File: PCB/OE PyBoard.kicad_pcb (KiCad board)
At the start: 4 copper layers, 33 x 41.9 mm, 57 parts, among them J3 USB4105-GF-A, J4 Conn_02x03_Odd_Even, J6 Conn_01x08, J7 Conn_01x08, U2 STM32F405RGT6, U3 MCP1700T, X2 12 MHz, X3 32.768 kHz

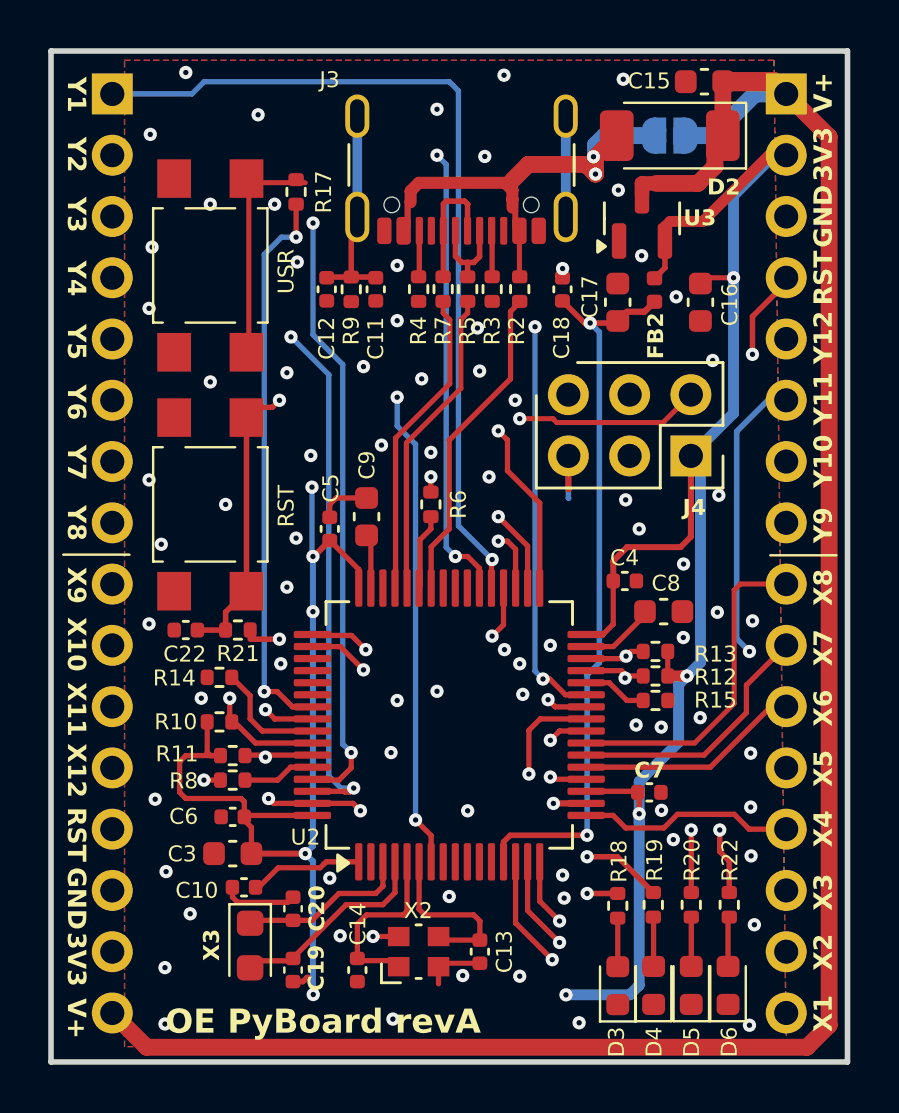
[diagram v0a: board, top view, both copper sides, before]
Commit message: Fixed cristal and diode's footprint.
Also, updated the production files.

Co-Authored-By: David Palma <78764277+davidpalma666@users.noreply.github.com>
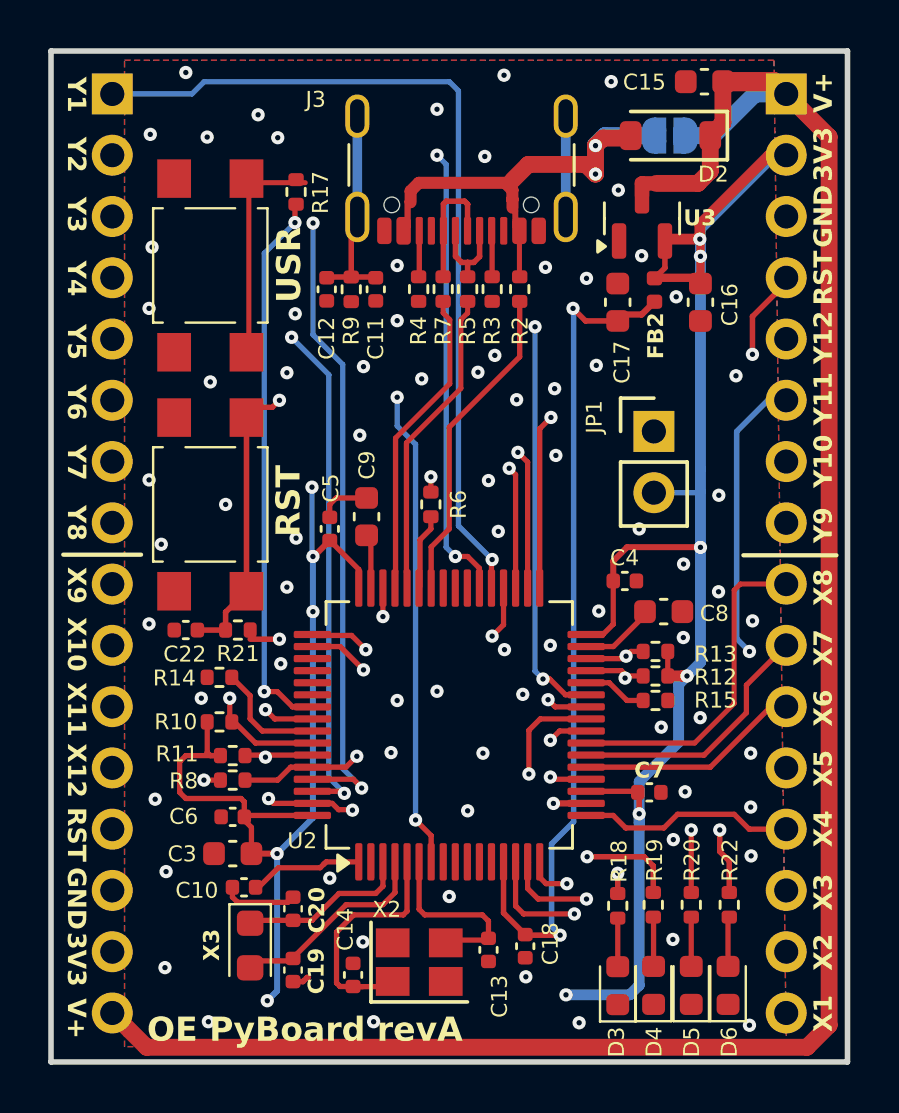
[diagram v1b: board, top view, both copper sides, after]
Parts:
- removed J4: Conn_02x03_Odd_Even, Connector_PinSocket_2.54mm:PinSocket_2x03_P2.54mm_Vertical
- added JP1: Jumper, Connector_PinHeader_2.54mm:PinHeader_1x02_P2.54mm_Vertical, F.Cu at (150.5, 110.0)
- D2: footprint Diode_SMD:D_SOD-128 -> Diode_SMD:D_SOD-123
- X2: footprint Crystal:Crystal_SMD_Abracon_ABM10-4Pin_2.5x2.0mm -> Crystal:Crystal_SMD_Abracon_ABM8AIG-4Pin_3.2x2.5mm
- moved C18 27.3 mm to (145.1, 131.3), turned to -90 degrees
- moved X2 0.43 mm to (140.7, 132.0), turned to 0 degrees
- moved C13 0.36 mm to (143.6, 131.5)
- moved C14 0.27 mm to (138.0, 132.5), turned to 90 degrees
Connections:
- net /PA14-JTCK renamed /PA14-GRN
- net /PA15-JTDI renamed /PA15-YEL
- net /PB4-NJTRST renamed /PB4-BLU
- R18 pad 1: /PB6-JTDO -> /PA13-RED
- U2 pad 46: /PA13-TMS -> /PA13-RED
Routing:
- net /BOOT0: track 3.01 -> 30.9 mm, vias 0 -> 2
- net /PB6-JTDO: track 23.2 -> 0.00 mm, vias 1 -> 0
- net /PA13-RED: track 0.00 -> 22.4 mm, vias 0 -> 3
- net /PA14-GRN: track 40.6 -> 23.8 mm, vias 4 -> 3
- net /PB4-BLU: track 40.4 -> 28.2 mm, vias 4 -> 3
- net /PA15-YEL: track 39.4 -> 27.7 mm, vias 4 -> 3
- net GND: track 19.9 -> 11.8 mm, vias 75 -> 72
- net /VDDA: track 30.5 -> 35.4 mm
- net /N3: track 7.12 -> 10.8 mm
- net /PB8-Y3: track 33.1 -> 35.8 mm
- net /PB13-Y6: track 21.5 -> 23.5 mm
- net /PB12-Y5: track 24.8 -> 26.8 mm
- net /PB14-Y7: track 19.8 -> 21.6 mm
- net +3V3: track 134.5 -> 135.9 mm, vias 11 -> 13
- net /PA2-X3: track 12.7 -> 11.5 mm
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
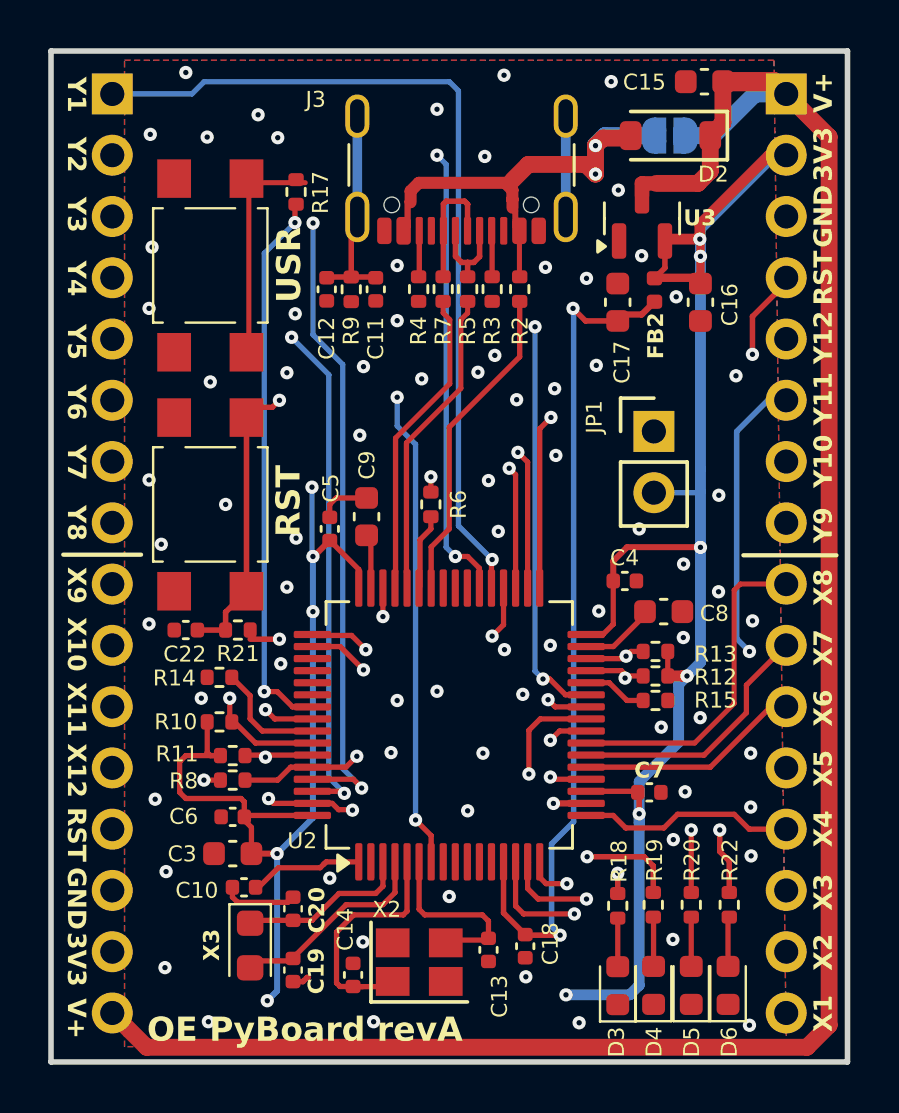
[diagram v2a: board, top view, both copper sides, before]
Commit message: Isolated used analog lines and moved buttons
Note: Gerbers and PnP files are not updated.
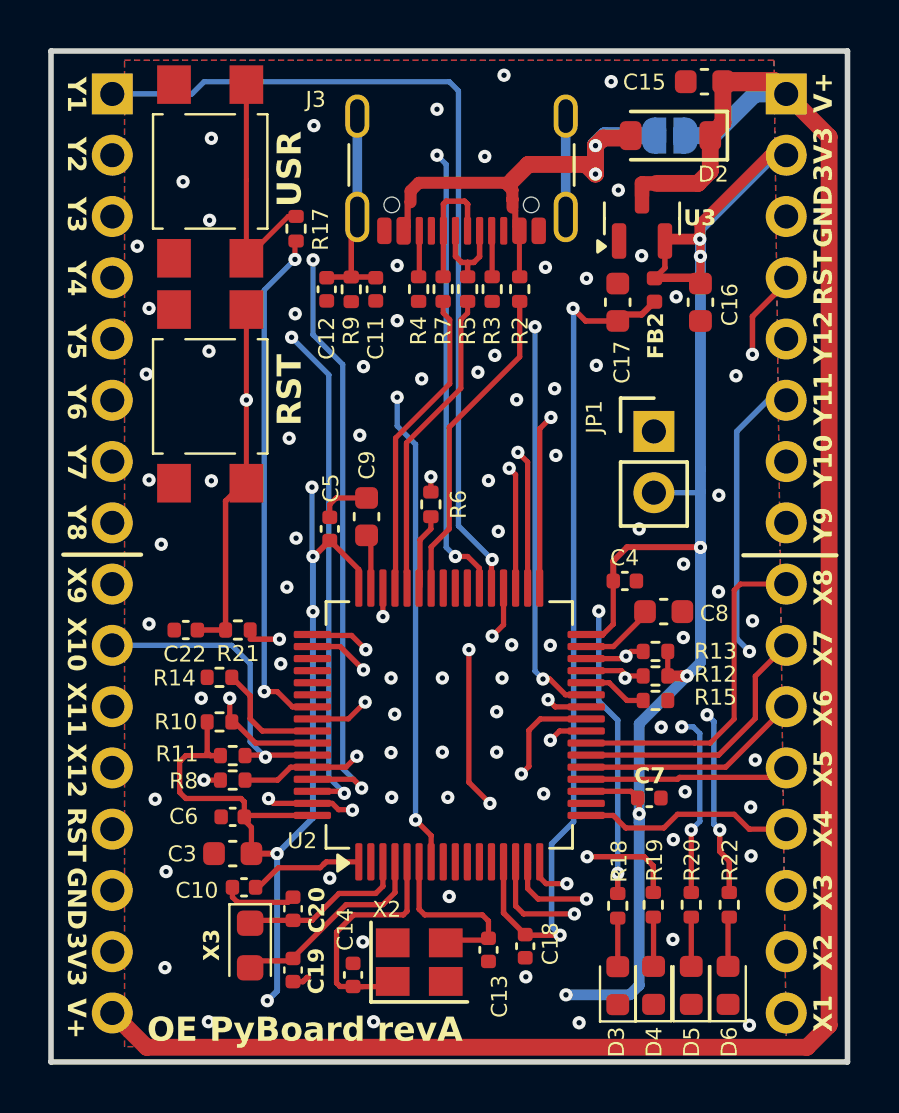
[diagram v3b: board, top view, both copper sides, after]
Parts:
- moved RST2 4.48 mm to (132.1, 108.5)
- moved USR2 3.90 mm to (132.1, 99.2)
- moved R17 1.53 mm to (135.6, 101.6)
- moved C7 0.23 mm to (150.3, 125.2)
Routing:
- net /RST-SW: track 68.4 -> 73.3 mm
- net /PB4-BLU: track 28.2 -> 25.0 mm
- net /PA4-X5: track 10.9 -> 9.03 mm, vias 1 -> 0
- net /PB3-SW1: track 22.9 -> 21.4 mm
- net GND: track 11.8 -> 10.4 mm, vias 72 -> 77
- net /PA14-GRN: track 23.8 -> 22.9 mm, vias 3 -> 4
- net /PA5-X6: track 8.70 -> 9.33 mm
- net /USR-SW: track 9.40 -> 9.98 mm
- net /PA15-YEL: track 27.7 -> 28.1 mm, vias 3 -> 4

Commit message: Updated production files.
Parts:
- moved REF** 0.85 mm to (142.0, 114.4)
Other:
- board text added: "For Research Use Only"
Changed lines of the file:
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@@
 			(layer "F.SilkS"
 				(type "Top Silk Screen")
-				(color "Black")
+				(color "White")
 				(material "Direct Printing")
 			)
@@
 			(layer "F.Mask"
 				(type "Top Solder Mask")
-				(color "White")
+				(color "Green")
 				(thickness 0.01)
 				(material "Epoxy")
@@
 			(layer "B.Mask"
 				(type "Bottom Solder Mask")
-				(color "White")
+				(color "Green")
 				(thickness 0.01)
 				(material "Epoxy")
@@
 			(layer "B.SilkS"
 				(type "Bottom Silk Screen")
-				(color "Black")
+				(color "White")
 				(material "Direct Printing")
 			)
@@
 	(footprint "OE PyBoard FootprintLib:OEPS Logo"
 		(layer "B.Cu")
-		(at 141.986 115.2652 180)
+		(at 141.975 114.4152 180)
 		(property "Reference" "REF**"
 			(at 0 0.5 0)
@@
 		)
 	)
+	(gr_text "For Research\nUse Only"
+		(at 141.975 130.3 0)
+		(layer "B.SilkS")
+		(effects
+			(font
+				(size 1.15 1.15)
+				(thickness 0.25)
+				(bold yes)
+			)
+			(justify bottom mirror)
+		)
+	)

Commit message: Removed board stackup table from F.Fab layer
Updated Gerber files to reflect these change.
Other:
- board text removed: "0"
- board text removed: "0 mm"
- board text removed: "0.01 mm"
- board text removed: "0.02"
- board text removed: "0.035 mm"
- board text removed: "1"
- board text removed: "1.51 mm"
- board text removed: "3.3"
- board text removed: "4.5"
- board text removed: "B.Cu"
- board text removed: "B.Mask"
- board text removed: "B.Paste"
- board text removed: "B.Silkscreen"
- board text removed: "Black"
- board text removed: "Bottom Silk Screen"
- board text removed: "Bottom Solder Mask"
- board text removed: "Bottom Solder Paste"
- board text removed: "Color"
- board text removed: "Dielectric 1"
- board text removed: "Epsilon R"
- board text removed: "F.Cu"
- board text removed: "F.Mask"
- board text removed: "F.Paste"
- board text removed: "F.Silkscreen"
- board text removed: "FR4"
- board text removed: "Layer Name"
- board text removed: "Loss Tangent"
- board text removed: "Material"
- board text removed: "Not specified"
- board text removed: "Polyimide"
- board text removed: "Thickness (mm)"
- board text removed: "Top Silk Screen"
- board text removed: "Top Solder Mask"
- board text removed: "Top Solder Paste"
- board text removed: "Type"
- board text removed: "White"
- board text removed: "copper"
- board text removed: "core"
